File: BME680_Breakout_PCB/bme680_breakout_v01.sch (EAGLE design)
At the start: 6 parts, among them IC1 BME680, X1 MICROMATCH-6

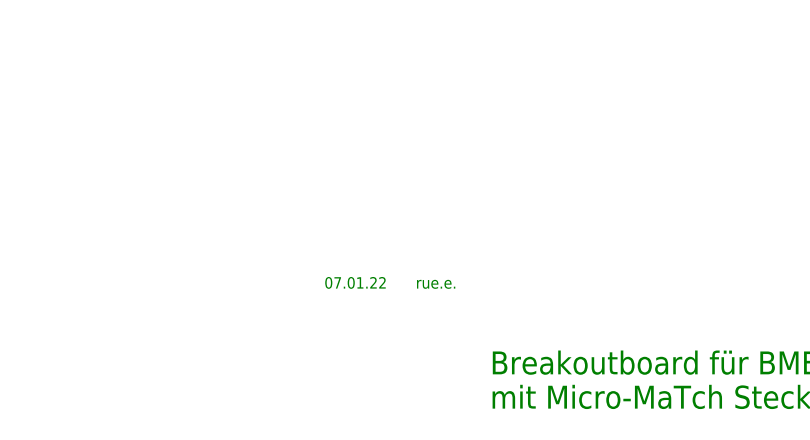
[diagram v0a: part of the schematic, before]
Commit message: change pcb color
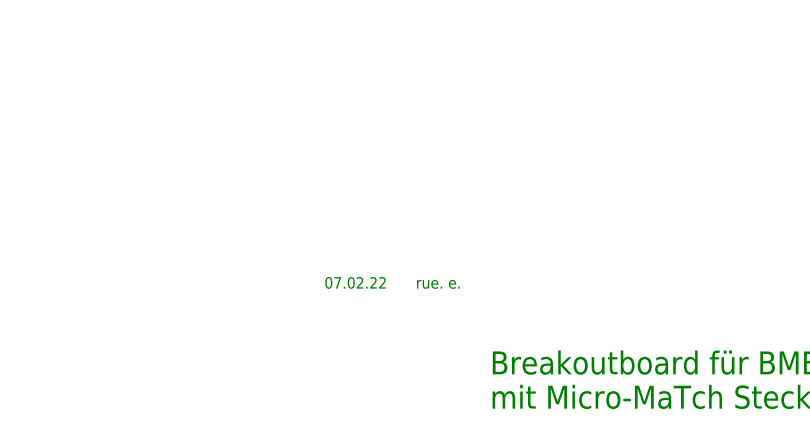
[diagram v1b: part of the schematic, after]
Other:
- note added: "07.02.22"
- note added: "rue. e."
- note removed: "07.01.22"
- note removed: "rue.e."
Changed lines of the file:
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@@
 <text x="363.22" y="40.64" size="2.54" layer="91" ratio="10">Breakoutboard für BME680
 mit Micro-MaTch Stecker</text>
-<text x="354.965" y="53.975" size="1.27" layer="91" ratio="10">rue.e.</text>
-<text x="344.805" y="53.975" size="1.27" layer="91" ratio="10">07.01.22</text>
+<text x="354.965" y="53.975" size="1.27" layer="91" ratio="10">rue. e.</text>
+<text x="344.805" y="53.975" size="1.27" layer="91" ratio="10">07.02.22</text>
 </plain>
 <instances>
